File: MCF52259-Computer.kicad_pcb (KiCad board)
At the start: 6 copper layers, 110.5 x 130 mm, 21 parts, among them J1 Conn_02x10_Counter_Clockwise, J2 Micro_SD_Card, Y1 8MHz

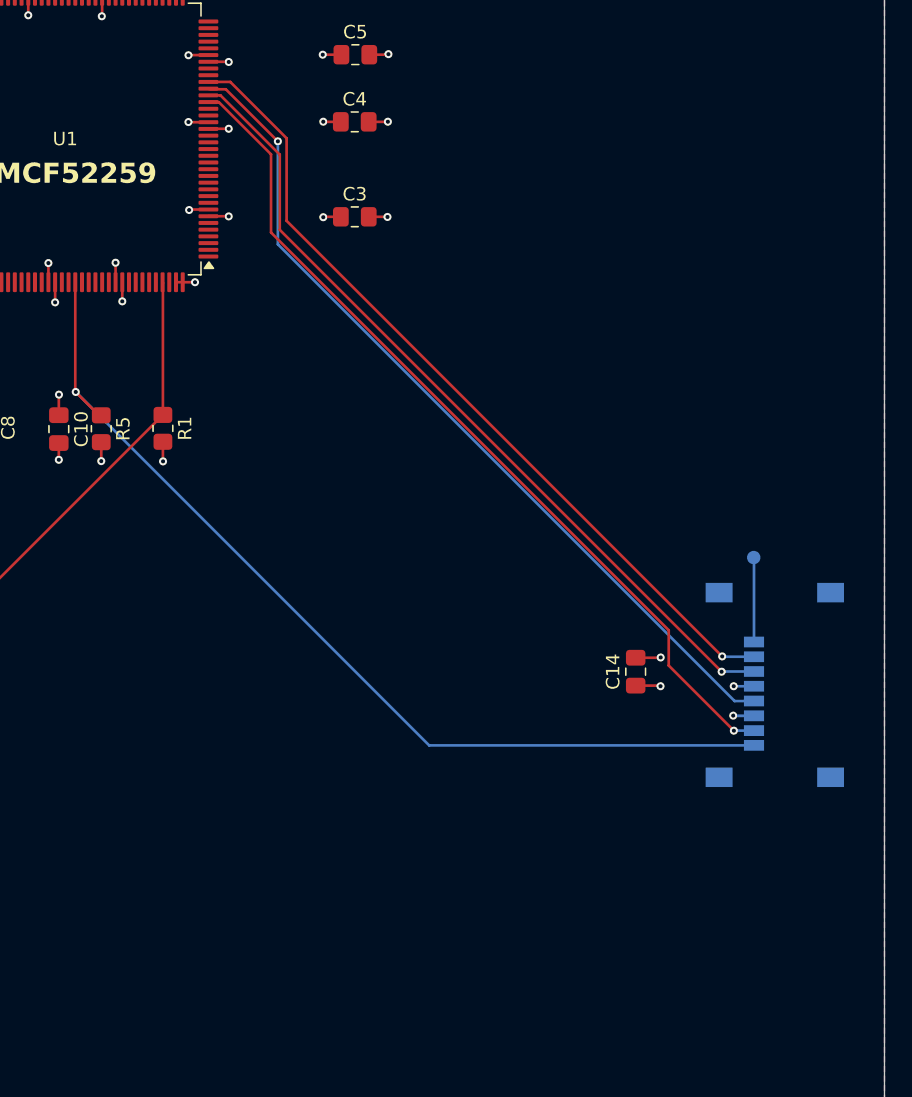
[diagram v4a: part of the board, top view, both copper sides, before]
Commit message: Added Second Micro SD-Card
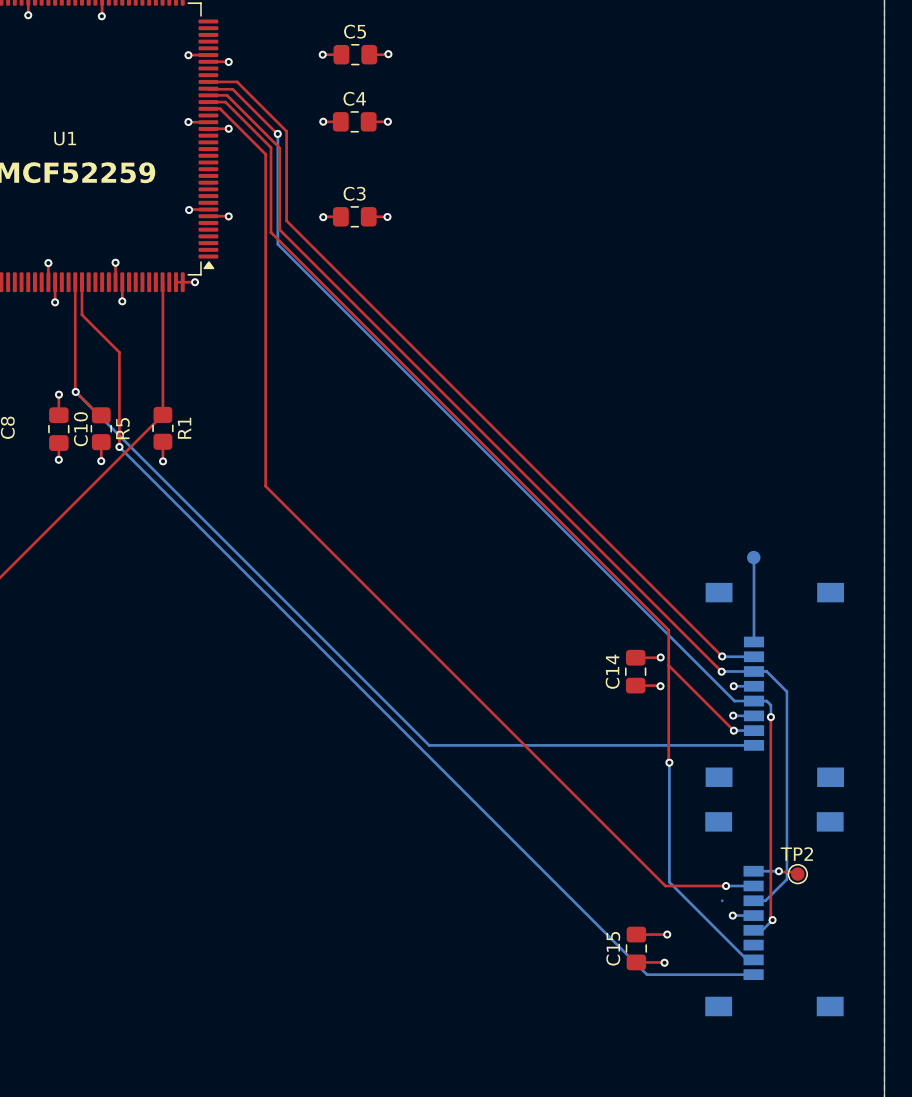
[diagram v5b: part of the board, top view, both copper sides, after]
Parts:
- added C15: 0.1µF, Capacitor_SMD:C_0805_2012Metric_Pad1.18x1.45mm_HandSolder, F.Cu at (146.1, 128.5)
- added J3: Micro_SD_Card, Connector_Card:microSD_HC_Wuerth_693072010801, B.Cu at (156.4, 126.0)
- added TP2: SD0_D2, TestPoint:TestPoint_Pad_D1.0mm, F.Cu at (158.1, 123.0)
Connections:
- net PCS3 renamed QSPI_CS3
- U1 pad 23: PCS2 -> QSPI_CS2
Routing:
- net QSPI_CS2: track 0.00 -> 79.0 mm, vias 0 -> 1
- net /IRQ3: track 0.00 -> 76.9 mm, vias 0 -> 1
- net QSPI_MISO: track 65.0 -> 90.1 mm, vias 1 -> 2
- net QSPI_MOSI: track 61.7 -> 82.2 mm
- net QSPI_CLK: track 63.9 -> 83.4 mm, vias 1 -> 3
- net VDD: track 37.5 -> 41.1 mm, vias 25 -> 27
- net Net-(J3-DAT2): track 0.00 -> 3.38 mm, vias 0 -> 1
- net VSS: track 37.1 -> 39.4 mm, vias 25 -> 26

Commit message: Added Neccesary Pull-Up to IRQ3
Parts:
- added R2: 22kΩ, Resistor_SMD:R_0805_2012Metric_Pad1.20x1.40mm_HandSolder, F.Cu at (154.8, 137.3)
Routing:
- net /IRQ3: track 76.9 -> 82.7 mm, vias 1 -> 2
- net VDD: track 41.1 -> 42.8 mm, vias 27 -> 28
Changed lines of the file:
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@@
 	(footprint "Resistor_SMD:R_0805_2012Metric_Pad1.20x1.40mm_HandSolder"
 		(layer "F.Cu")
+		(at 154.8 137.3 -90)
+		(descr "Resistor SMD 0805 (2012 Metric), square (rectangular) end terminal, IPC-7351 nominal with elongated pad for handsoldering. (Body size source: IPC-SM-782 page 72, https://www.pcb-3d.com/wordpress/wp-content/uploads/ipc-sm-782a_amendment_1_and_2.pdf), generated with kicad-footprint-generator")
+		(tags "resistor handsolder")
+		(property "Reference" "R2"
+			(at 0 -1.65 90)
+			(layer "F.SilkS")
+			(effects
+				(font
+					(size 1 1)
+					(thickness 0.15)
+				)
+			)
+		)
+		(property "Value" "22kΩ"
+			(at 0 1.65 90)
+			(layer "F.Fab")
+			(effects
+				(font
+					(size 1 1)
+					(thickness 0.15)
+				)
+			)
+		)
+		(property "Datasheet" ""
+			(at 0 0 90)
+			(layer "F.Fab")
+			(hide yes)
+			(effects
+				(font
+					(size 1.27 1.27)
+					(thickness 0.15)
+				)
+			)
+		)
+		(property "Description" "Resistor"
+			(at 0 0 90)
+			(layer "F.Fab")
+			(hide yes)
+			(effects
+				(font
+					(size 1.27 1.27)
+					(thickness 0.15)
+				)
+			)
+		)
+		(property ki_fp_filters "R_*")
+		(sheetname "/")
+		(sheetfile "MCF52259-Computer.kicad_sch")
+		(attr smd)
+		(fp_line
+			(start -0.227064 0.735)
+			(end 0.227064 0.735)
+			(stroke
+				(width 0.12)
+				(type solid)
+			)
+			(layer "F.SilkS")
+		)
+		(fp_line
+			(start -0.227064 -0.735)
+			(end 0.227064 -0.735)
+			(stroke
+				(width 0.12)
+				(type solid)
+			)
+			(layer "F.SilkS")
+		)
+		(fp_line
+			(start -1.85 0.95)
+			(end -1.85 -0.95)
+			(stroke
+				(width 0.05)
+				(type solid)
+			)
+			(layer "F.CrtYd")
+		)
+		(fp_line
+			(start 1.85 0.95)
+			(end -1.85 0.95)
+			(stroke
+				(width 0.05)
+				(type solid)
+			)
+			(layer "F.CrtYd")
+		)
+		(fp_line
+			(start -1.85 -0.95)
+			(end 1.85 -0.95)
+			(stroke
+				(width 0.05)
+				(type solid)
+			)
+			(layer "F.CrtYd")
+		)
+		(fp_line
+			(start 1.85 -0.95)
+			(end 1.85 0.95)
+			(stroke
+				(width 0.05)
+				(type solid)
+			)
+			(layer "F.CrtYd")
+		)
+		(fp_line
+			(start -1 0.625)
+			(end -1 -0.625)
+			(stroke
+				(width 0.1)
+				(type solid)
+			)
+			(layer "F.Fab")
+		)
+		(fp_line
+			(start 1 0.625)
+			(end -1 0.625)
+			(stroke
+				(width 0.1)
+				(type solid)
+			)
+			(layer "F.Fab")
+		)
+		(fp_line
+			(start -1 -0.625)
+			(end 1 -0.625)
+			(stroke
+				(width 0.1)
+				(type solid)
+			)
+			(layer "F.Fab")
+		)
+		(fp_line
+			(start 1 -0.625)
+			(end 1 0.625)
+			(stroke
+				(width 0.1)
+				(type solid)
+			)
+			(layer "F.Fab")
+		)
+		(fp_text user "${REFERENCE}"
+			(at 0 0 90)
+			(layer "F.Fab")
+			(effects
+				(font
+					(size 0.5 0.5)
+					(thickness 0.08)
+				)
+			)
+		)
+		(pad "1" smd roundrect
+			(at -1 0 270)
+			(size 1.2 1.4)
+			(layers "F.Cu" "F.Mask" "F.Paste")
+			(roundrect_rratio 0.208333)
+			(net 4 "{slash}IRQ3")
+			(pintype "passive")
+		)
+		(pad "2" smd roundrect
+			(at 1 0 270)
+			(size 1.2 1.4)
+			(layers "F.Cu" "F.Mask" "F.Paste")
+			(roundrect_rratio 0.208333)
+			(net 12 "VDD")
+			(pintype "passive")
+		)
+		(embedded_fonts no)
+		(model "${KICAD9_3DMODEL_DIR}/Resistor_SMD.3dshapes/R_0805_2012Metric.step"
+			(offset
+				(xyz 0 0 0)
+			)
+			(scale
+				(xyz 1 1 1)
+			)
+			(rotate
+				(xyz 0 0 0)
+			)
+		)
+	)
+	(footprint "Resistor_SMD:R_0805_2012Metric_Pad1.20x1.40mm_HandSolder"
+		(layer "F.Cu")
 		(at 106.26 89.84 -90)
 		(descr "Resistor SMD 0805 (2012 Metric), square (rectangular) end terminal, IPC-7351 nominal with elongated pad for handsoldering. (Body size source: IPC-SM-782 page 72, https://www.pcb-3d.com/wordpress/wp-content/uploads/ipc-sm-782a_amendment_1_and_2.pdf), generated with kicad-footprint-generator")
@@
 	)
 	(segment
+		(start 154.8 133.8)
+		(end 154.8 136.3)
+		(width 0.2)
+		(layer "F.Cu")
+		(net 4)
+	)
+	(segment
 		(start 107.61147 84.15147)
 		(end 104.82 81.36)
@@
 		(net 4)
 	)
+	(via
+		(at 154.8 133.8)
+		(size 0.6)
+		(drill 0.3)
+		(layers "F.Cu" "B.Cu")
+		(net 4)
+	)
+	(segment
+		(start 154.8 130.515)
+		(end 154.83 130.485)
+		(width 0.2)
+		(layer "B.Cu")
+		(net 4)
+	)
 	(segment
 		(start 146.89647 130.485)
@@
 	)
 	(segment
+		(start 154.8 133.8)
+		(end 154.8 130.515)
+		(width 0.2)
+		(layer "B.Cu")
+		(net 4)
+	)
+	(segment
 		(start 116.3775 64.0175)
 		(end 114.2375 64.0175)
@@
 	)
 	(segment
+		(start 154.8 138.3)
+		(end 154.8 140)
+		(width 0.2)
+		(layer "F.Cu")
+		(net 12)
+	)
+	(segment
 		(start 124.14 61.99)
 		(end 122.75 61.99)
@@
 		(size 0.6)
 		(drill 0.3)
+		(layers "F.Cu" "B.Cu")
+		(net 12)
+	)
+	(via
+		(at 154.8 140)
+		(size 0.6)
+		(drill 0.3)
